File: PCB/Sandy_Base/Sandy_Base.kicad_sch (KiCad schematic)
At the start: 163 parts, among them J1 Conn_02x02_Top_Bottom, J10 Conn_01x03, J2 Conn_02x02_Top_Bottom, J3 Conn_02x02_Top_Bottom, J4 Conn_02x02_Top_Bottom, J5 Conn_02x02_Top_Bottom, J6 Conn_02x02_Top_Bottom, J7 USB_C_Receptacle_USB2.0, J8 Conn_02x03_Odd_Even, J9 Conn_01x02, U1 ATmega32U4-MU, U2 24LC64, Y1 16MHz

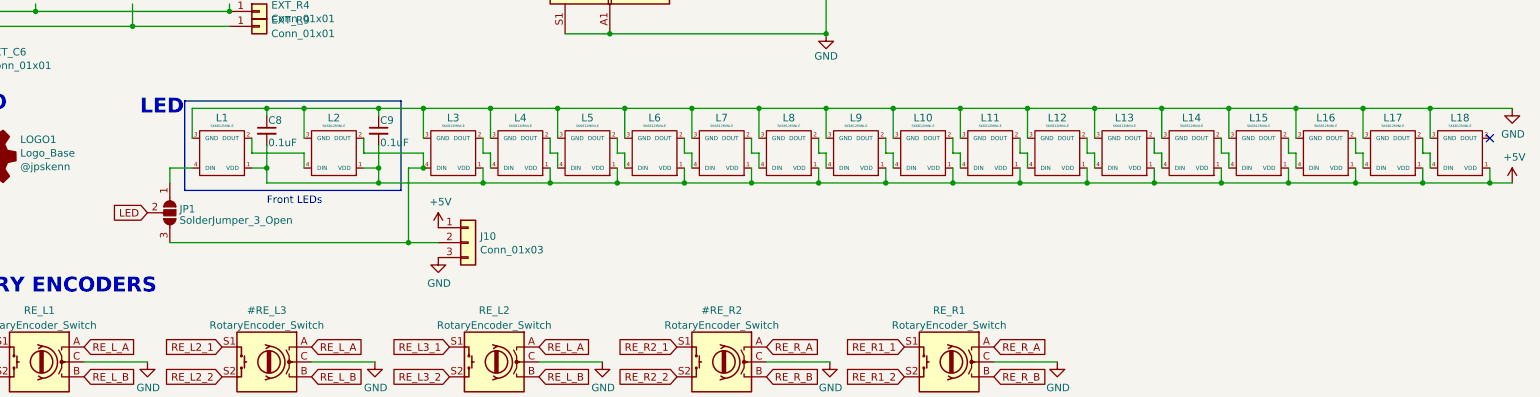
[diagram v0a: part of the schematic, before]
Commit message: WIP ネジ穴位置、スイッチ位置調整中
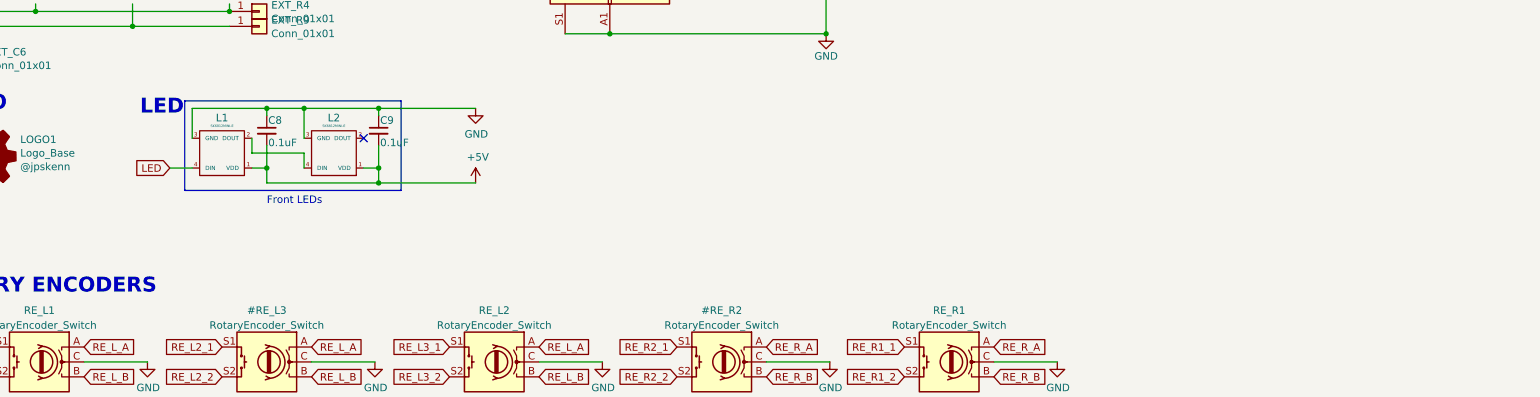
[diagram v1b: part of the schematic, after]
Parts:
- removed J10: Conn_01x03, Connector_PinHeader_2.54mm:PinHeader_1x03_P2.54mm_Vertical, symbol Connector_Generic:Conn_01x03
- removed JP1: SolderJumper_3_Open, Jumper:SolderJumper-3_P1.3mm_Open_RoundedPad1.0x1.5mm, symbol Jumper:SolderJumper_3_Open
- removed L10, L11, L12, L13, L14, L15, L16, L17, L18, L3, L4, L5, L6, L7, L8, L9: SK6812MINI-E, locallib:YS-SK6812MINI-E_middle_hole_with_small_pad, symbol kbd:SK6812MINI-E
- SW_CTL1, SW_ENT1: footprint MX_Alps_Hybrid:MXOnly-1.5U-Hotswap-guide -> MX_Alps_Hybrid:MXOnly-1U-Hotswap-guide
- SW_LALTu1, SW_LWIN1, SW_RALT1, SW_RWIN1: footprint MX_Alps_Hybrid:MXOnly-1.25U-Hotswap-guide -> MX_Alps_Hybrid:MXOnly-1U-Hotswap-guide
- SW_LSPC1: footprint MX_Alps_Hybrid:MXOnly-2U-Hotswap-guide2 -> MX_Alps_Hybrid:MXOnly-1.25U-Hotswap-guide
- SW_RSPC1: footprint MX_Alps_Hybrid:MXOnly-1.5U-Hotswap-guide -> MX_Alps_Hybrid:MXOnly-1.25U-Hotswap-guide
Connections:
- net LED: now also L1.4 (DIN)

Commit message: 不要なロータリーエンコーダを削除。電源シンボル更新。
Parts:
- removed #RE_L3, #RE_R2, RE_L2, RE_R1: RotaryEncoder_Switch, locallib:RotaryEncoder_Alps_EC11K-Switch_Vertical_H20mm_NPTH_MP_minimal, symbol Device:RotaryEncoder_Switch
- J7: symbol Connector:USB_C_Receptacle_USB2.0 -> Connector:USB_C_Receptacle_USB2.0_16P
- renumbered RE_L1 to RE_Base1
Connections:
- net RE_L1_1 is gone; now on net MISO: RE_Base1.S1
- net RE_L3_2 is gone; now on net RE_Base1_S2: D33.2 (A), SW_R5CNT_C1.2
- net RE_L1_2 renamed RE_Base1_S2
- net RE_L2_2: no longer names the net of D32.2 (A), SW_R5CNT_L1.2
- net RE_L_A: no longer names the net of U1.39 (PF4)
- net RE_L_A: no longer RE_Base1.A
- net RE_L_B: no longer names the net of U1.40 (PF1)
- net RE_L_B: no longer RE_Base1.B
- net RE_R2_1 renamed col4
- net RE_R2_2: no longer names the net of D34.2 (A), SW_R5CNT_R1.2
- net RE_R_A renamed RE_Base1_A
- net RE_Base1_A: now also RE_Base1.A
- net RE_R_B renamed RE_Base1_B
- net RE_Base1_B: now also RE_Base1.B
- no-connect marks 7 -> 9
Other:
- note removed: "Front LEDs"
- moved on the sheet: C8, C9, H10, H11, H12, H13, H14, H40, H41, H6, H7, H8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

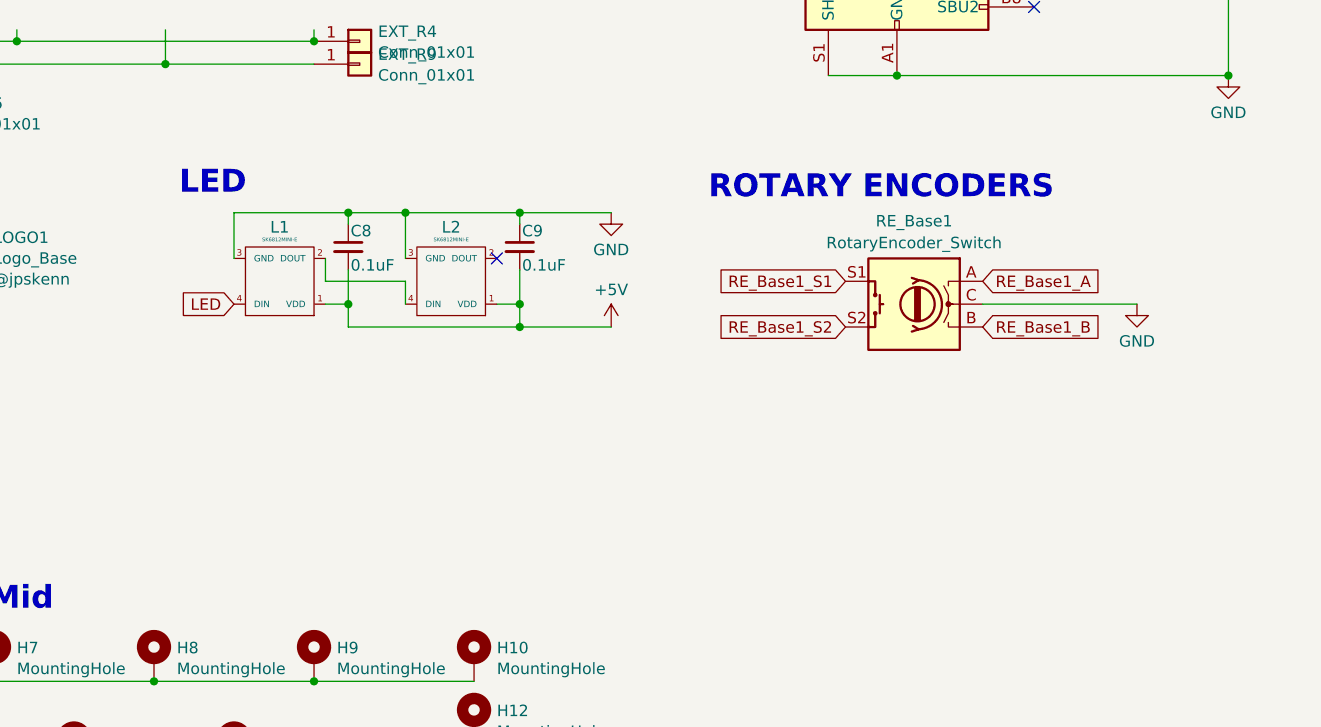
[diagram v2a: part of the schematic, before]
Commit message: LEDを2個増やして4個にした
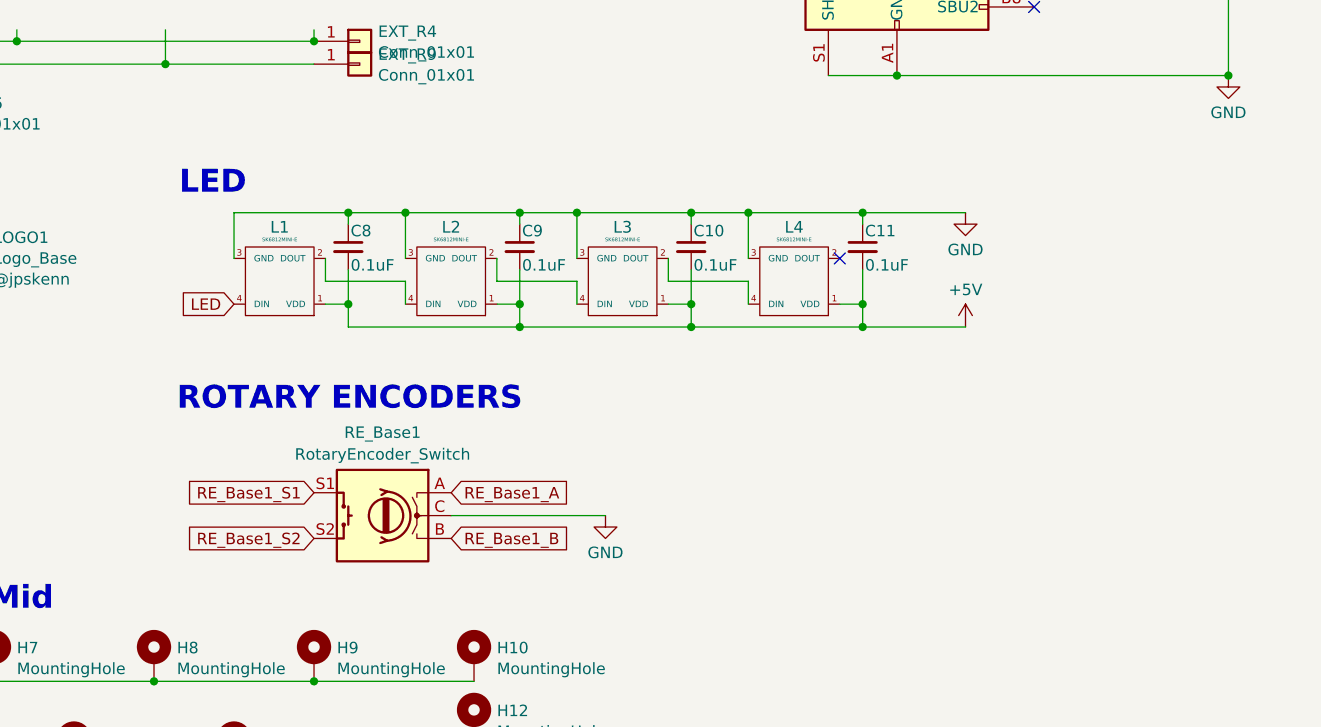
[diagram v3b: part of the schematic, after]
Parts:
- added C10, C11: 0.1uF, Capacitor_SMD:C_0805_2012Metric, symbol Device:C_Small
- added L3, L4: SK6812MINI-E, locallib:YS-SK6812MINI-E_middle_hole_with_small_pad, symbol kbd:SK6812MINI-E
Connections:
- net +5V: now also C10.2, C11.2, L3.1 (VDD), L4.1 (VDD)
- net GND: now also C10.1, C11.1, L3.3 (GND), L4.3 (GND)
- net at L2.2 (DOUT): now also L3.4 (DIN)
- new net: L3.2 (DOUT), L4.4 (DIN)
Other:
- moved on the sheet: RE_Base1

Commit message: MCU置き換え
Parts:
- removed J8: Conn_02x03_Odd_Even, Connector_PinHeader_2.54mm:PinHeader_2x03_P2.54mm_Vertical, symbol Connector_Generic:Conn_02x03_Odd_Even
- removed J9: Conn_01x02, Connector_PinHeader_2.54mm:PinHeader_1x02_P2.54mm_Vertical, symbol Connector_Generic:Conn_01x02
- removed R8, R9: 4.7k, Resistor_SMD:R_0805_2012Metric, symbol Device:R
- removed ResetSW1: 5.2x5.2mm, Button_Switch_SMD:SW_SPST_TL3342, symbol Sandy-rescue:SW_Push-Jones-rescue
- removed U1: ATmega32U4-MU, Package_DFN_QFN:QFN-44-1EP_7x7mm_P0.5mm_EP5.2x5.2mm, symbol Sandy-rescue:ATmega32U4-MU-MCU_Microchip_ATmega
- removed U2: 24LC64, Package_SO:SO-8_3.9x4.9mm_P1.27mm, symbol Memory_EEPROM:24LC64
- removed Y1: 16MHz, Crystal:Crystal_SMD_3225-4Pin_3.2x2.5mm_HandSoldering, symbol Device:Crystal_GND24
- added C12, C13, C14, C15, C18: 100n, Capacitor_SMD:C_0402_1005Metric, symbol Device:C_Small
- added C16, C17, C19: 2.2uF, Capacitor_SMD:C_0402_1005Metric, symbol Device:C_Small
- added J10: TP3, Connector_PinHeader_2.54mm:PinHeader_1x01_P2.54mm_Vertical, symbol Connector_Generic:Conn_01x01
- added J8: TP1, Connector_PinHeader_2.54mm:PinHeader_1x01_P2.54mm_Vertical, symbol Connector_Generic:Conn_01x01
- added J9: TP2, Connector_PinHeader_2.54mm:PinHeader_1x01_P2.54mm_Vertical, symbol Connector_Generic:Conn_01x01
- added R10, R8: 1k, Resistor_SMD:R_0402_1005Metric, symbol Device:R_Small
- added R7: 27, Resistor_SMD:R_0402_1005Metric, symbol Device:R_Small
- added R9: 10k, Resistor_SMD:R_0402_1005Metric, symbol Device:R_Small
- added SD1: Schottky diode, Diode_SMD:D_SOD-123, symbol Device:D_Shockley
- added STLED1: LED_GREEN, LED_SMD:LED_0402_1005Metric, symbol Device:LED_Small
- added SW1: BOOT, Button_Switch_SMD:SW_SPST_PTS810, symbol Switch:SW_Push
- added SW2: RESET, Button_Switch_SMD:SW_SPST_PTS810, symbol Switch:SW_Push
- added U1: NCP1117-3.3_SOT223, Package_TO_SOT_SMD:SOT-223-3_TabPin2, symbol Regulator_Linear:NCP1117-3.3_SOT223
- added U2: RP2040, Package_DFN_QFN:QFN-56-1EP_7x7mm_P0.4mm_EP3.2x3.2mm, symbol MCU_RaspberryPi:RP2040
- added U3: W25Q128JVPIQ, Package_SON:WSON-8-1EP_6x5mm_P1.27mm_EP3.4x4.3mm, symbol Memory_Flash:W25Q128JVS
- added Y1: 12MHz, Crystal:Resonator_SMD_Murata_CSTxExxV-3Pin_3.0x1.1mm, symbol Device:Crystal_GND2
- C1: value 10uF -> 10u; footprint Capacitor_SMD:C_0805_2012Metric -> Capacitor_SMD:C_1206_3216Metric; LCSC C15850 -> C77090
- C10, C11, C4, C5, C7, C8, C9: value 0.1uF -> 100n; footprint Capacitor_SMD:C_0805_2012Metric -> Capacitor_SMD:C_0402_1005Metric; LCSC C49678 -> C1525
- C2: value 22pF -> 10u; footprint Capacitor_SMD:C_0805_2012Metric -> Capacitor_SMD:C_1206_3216Metric; LCSC C1804 -> C77090
- C3: value 22pF -> 100n; footprint Capacitor_SMD:C_0805_2012Metric -> Capacitor_SMD:C_0402_1005Metric; LCSC C1804 -> C1525
- C6: value 1uF -> 100n; footprint Capacitor_SMD:C_0805_2012Metric -> Capacitor_SMD:C_0402_1005Metric; LCSC C28323 -> C1525
- D1, D10, D11, D12, D13, D14, D16, D17, D18, D19, D2, D20, D21, D22, D23, D24, D25, D29, D3, D30, D31, D32, D33, D34, D35, D36, D37, D4, D5, D6, D7, D8, D9: LCSC C81598 -> C109203
- F1: value 500mA -> Fuse; footprint Fuse:Fuse_1206_3216Metric_Pad1.42x1.75mm_HandSolder -> Fuse:Fuse_0603_1608Metric; LCSC C70076 -> C187605
- R1, R2: footprint Resistor_SMD:R_0805_2012Metric -> Resistor_SMD:R_0402_1005Metric; LCSC C27834 -> C25905
- R3, R4: value 22 -> 27; footprint Resistor_SMD:R_0805_2012Metric -> Resistor_SMD:R_0402_1005Metric; LCSC C17561 -> C25100
- R5: value 10k -> 1k; footprint Resistor_SMD:R_0805_2012Metric -> Resistor_SMD:R_0402_1005Metric; LCSC C17414 -> C11702
- R6: value 10k -> 27; footprint Resistor_SMD:R_0805_2012Metric -> Resistor_SMD:R_0402_1005Metric; LCSC C17414 -> C25100
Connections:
- net +5V: now also C1.1, SD1.1 (K), U1.3 (VI); no longer C1.2, C4.2, C5.2, C7.2, F1.1, R5.1
- net D+: now also R4.1, R6.2; no longer R3.1
- net D-: now also R3.1, R7.2; no longer R4.1
- net GND: now also C1.2, C4.2, C5.2, C7.2, R1.2, R2.2, C12.2, C13.2, C14.2, C15.2, C16.2, C17.2, C18.2, C19.2, J9.1 (Pin_1), STLED1.1 (K), SW1.2, SW2.2, U1.1 (GND), U2.19 (TESTEN), U2.57 (GND), U3.4 (GND), Y1.2; no longer C1.1, C4.1, C5.1, C7.1, R1.1, R2.1, R6.1
- net LED: now also U2.11 (GPIO8)
- net RESET: now also SW2.1, U2.26 (RUN); no longer R5.2
- net RE_Base1_A: now also U2.8 (GPIO6)
- net RE_Base1_B: now also U2.9 (GPIO7)
- net col0: now also U2.30 (GPIO19)
- net col4: now also U2.35 (GPIO23)
- net col5: now also U2.36 (GPIO24)
- net col6: now also U2.37 (GPIO25)
- net row0: now also U2.12 (GPIO9)
- net row1: now also U2.13 (GPIO10)
- net row2: now also U2.14 (GPIO11)
- net row3: now also U2.15 (GPIO12)
- net row4: now also U2.16 (GPIO13)
- net row5: now also U2.17 (GPIO14)
- net row6: now also U2.18 (GPIO15)
- net row7: now also U2.27 (GPIO16)
- net row8: now also U2.28 (GPIO17)
- net row9: now also U2.29 (GPIO18)
- net +3V3: now reaches C6.1
- net +3V3: now also C2.1, C5.1, C7.1, R5.2, C12.1, C13.1, C14.1, C15.1, C17.1, C18.1, C19.1, R9.1, U1.2 (VO), U2.1 (IOVDD), U2.10 (IOVDD), U2.22 (IOVDD), U2.33 (IOVDD), U2.42 (IOVDD), U2.43 (ADC_AVDD), U2.44 (VREG_IN), U2.48 (USB_VDD), U2.49 (IOVDD), U3.8 (VCC)
- net +1V1: now reaches C3.1
- net +1V1: now also C4.1, C16.1, U2.23 (DVDD), U2.45 (VREG_VOUT), U2.50 (DVDD)
- net at D99.3 (I/O2), J7.A7 (D-), J7.B7 (D-): now also R3.2; no longer R4.2
- net at D99.2 (I/O1), J7.A6 (D+), J7.B6 (D+): now also R4.2; no longer R3.2
- net at J7.B5 (CC2): now also R2.1; no longer R1.2
- net at J7.A5 (CC1): now also R1.1; no longer R2.2
- net at D32.2 (A), SW_R5CNT_L1.2: now also RE_Base1.S2
- net MISO renamed col3
- net col3: now also U2.34 (GPIO22); no longer RE_Base1.S1
- net MOSI renamed col2
- net col2: now also RE_Base1.S1, U2.32 (GPIO21)
- net RE_Base1_S2: no longer names the net of D33.2 (A), SW_R5CNT_C1.2
- net RE_Base1_S2: no longer RE_Base1.S2
- net SCK renamed col1
- net col1: now also U2.31 (GPIO20)
- net VCC renamed VBUS
- net VBUS: now also F1.1; no longer F1.2
- new net: R6.1, U2.47 (USB_DP)
- new net: U2.20 (XIN), Y1.1
- new net: R8.1, Y1.3
- new net: R5.1, STLED1.2 (A)
- new net: R7.1, U2.46 (USB_DM)
- new net: R8.2, U2.21 (XOUT)
- new net: F1.2, SD1.2 (A)
- new net QSPI_SCLK: U2.52 (QSPI_SCLK), U3.6 (CLK)
- new net QSPI_SD0: U2.53 (QSPI_SD0), U3.5 (DI(IO0))
- new net QSPI_SD1: U2.55 (QSPI_SD1), U3.2 (DO(IO1))
- new net QSPI_SD2: U2.54 (QSPI_SD2), U3.3 (IO2)
- new net QSPI_SD3: U2.51 (QSPI_SD3), U3.7 (IO3)
- new net QSPI_SS: R10.2, R9.2, U2.56 (QSPI_SS), U3.1 (~{CS})
- new net SWCLK: J8.1 (Pin_1), U2.24 (SWCLK)
- new net SWD: J10.1 (Pin_1), U2.25 (SWD)
- new net USB_BOOT: R10.1, SW1.1
- no-connect marks 9 -> 17
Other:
- note added: "44PIN"
- note added: "45PIN"
- note removed: "Audio C4,5,6 B5,6,7"
- note removed: "EEPROM"
- note removed: "I2C"
- note removed: "ICSP"
- note removed: "ROTARY ENCODERS"
- moved on the sheet: D1, D10, D11, D12, D13, D14, D16, D17, D18, D19, D2, D20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

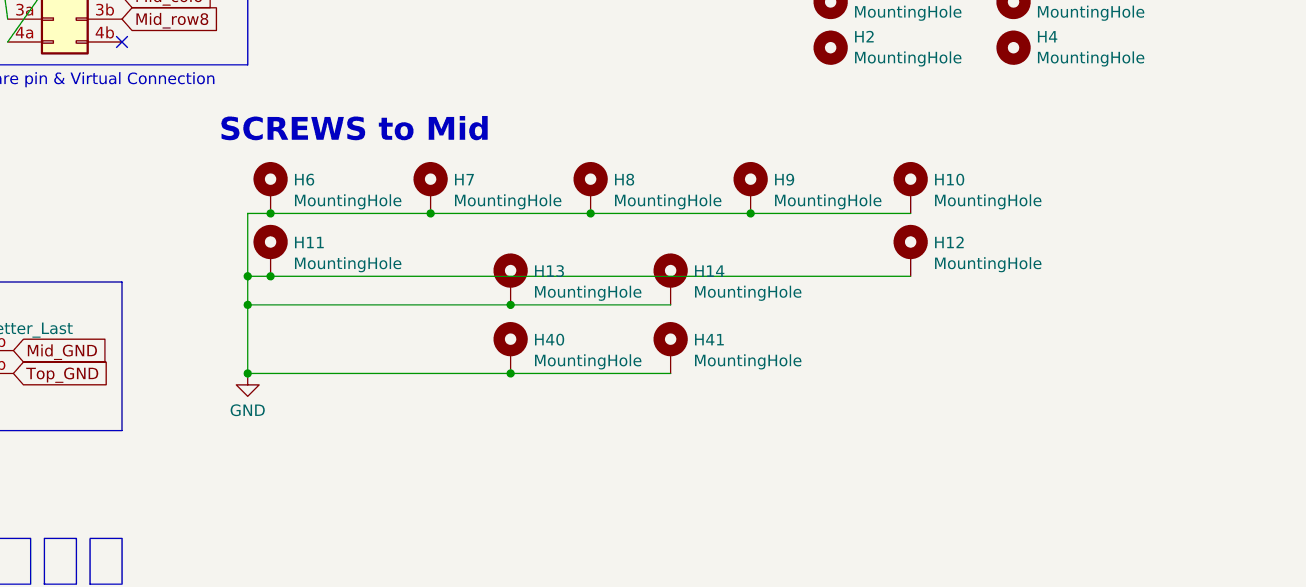
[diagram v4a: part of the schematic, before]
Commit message: ネジ穴調整、追加
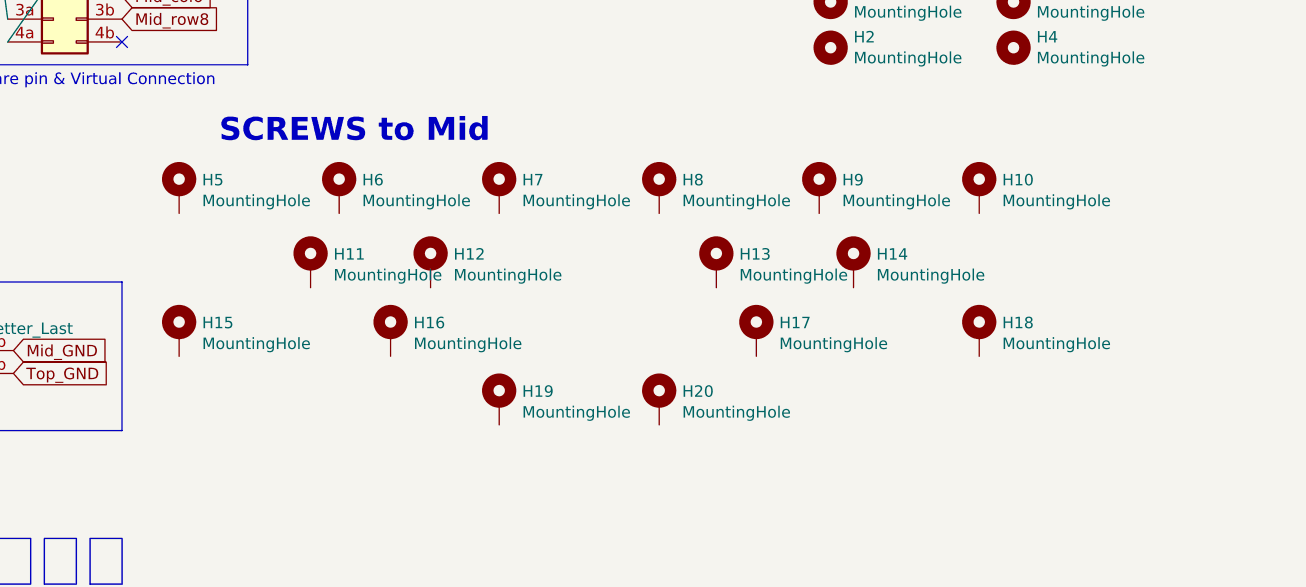
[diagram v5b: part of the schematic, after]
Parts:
- added H10, H11, H12, H13, H14: MountingHole, locallib:MountingHole_2.2mm_M2_Pad_minimal, symbol Mechanical:MountingHole_Pad
- renumbered H11 to H15, H13 to H16, H14 to H17, H12 to H18, H40 to H19, H41 to H20, H6 to H5, H7 to H6, H8 to H7, H9 to H8, H10 to H9
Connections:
- net GND: no longer H15.1, H16.1, H17.1, H18.1, H19.1, H20.1, H5.1, H6.1, H7.1, H8.1, H9.1
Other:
- moved on the sheet: H15, H16, H17, H18, H19, H20, H5, H6, H7, H8, H9
